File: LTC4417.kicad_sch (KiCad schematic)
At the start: 26 parts, among them Q4 IRF7324, Q5 IRF7324, Q6 IRF7324, Q7 IRF7324, U4 LTC4417CGN

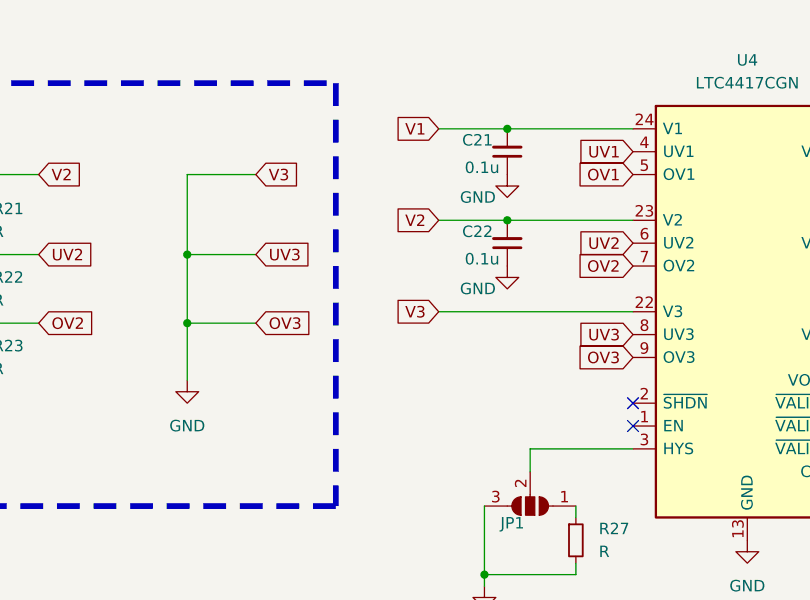
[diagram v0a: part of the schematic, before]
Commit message: LTC4088の修正必須
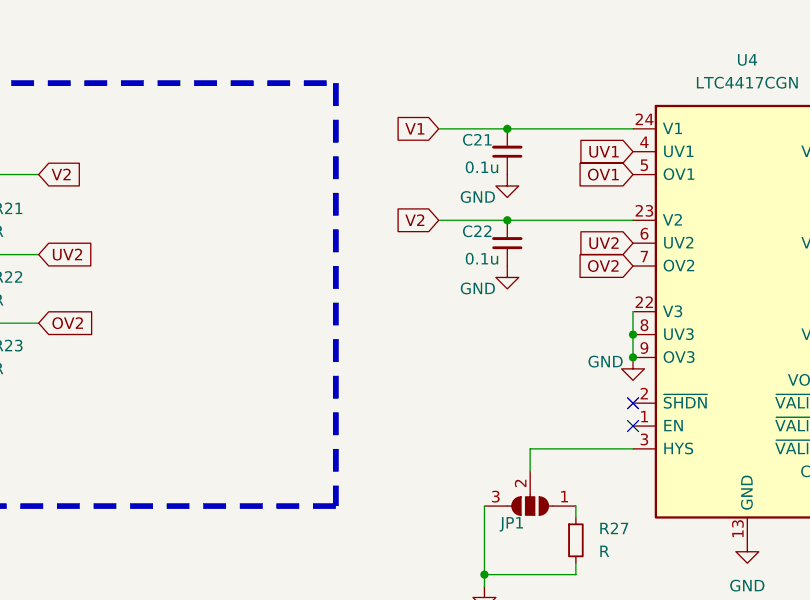
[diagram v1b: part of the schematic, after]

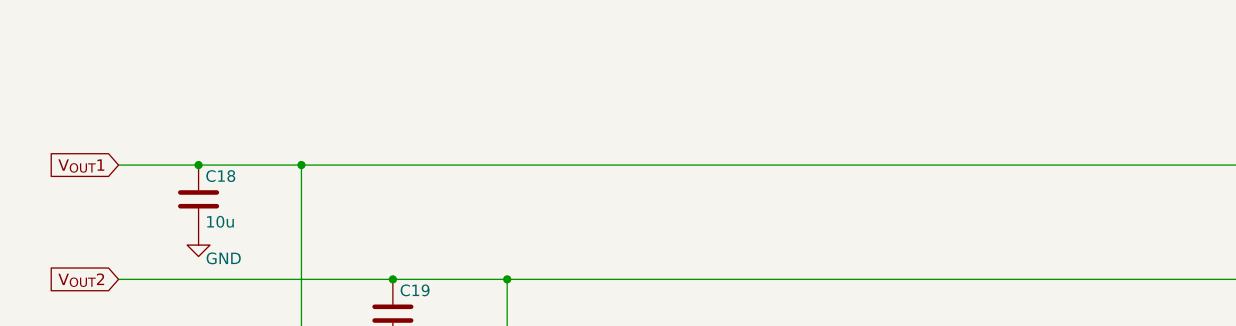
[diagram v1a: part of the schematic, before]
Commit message: add block image
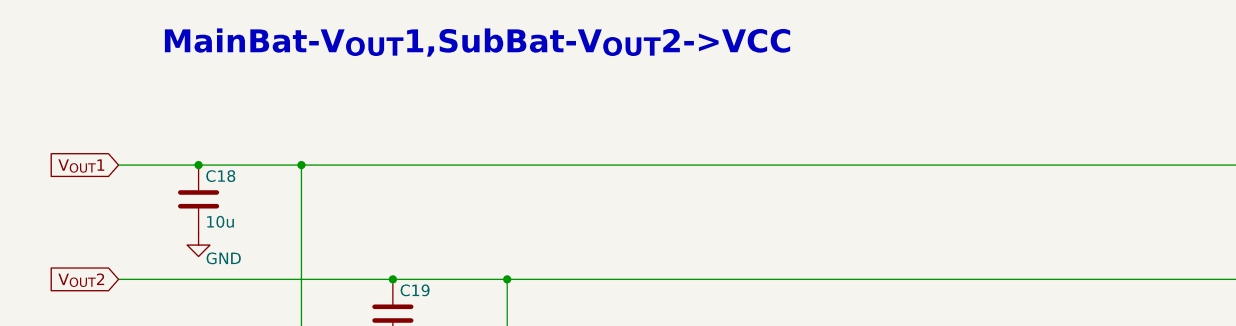
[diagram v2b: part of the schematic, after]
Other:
- note added: "MainBat-V_{OUT}1,SubBat-V_{OUT}2->VCC"
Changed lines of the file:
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@@
+		)
+	)
+	(text "MainBat-V_{OUT}1,SubBat-V_{OUT}2->VCC"
+		(exclude_from_sim no)
+		(at 32.766 25.908 0)
+		(effects
+			(font
+				(size 2.54 2.54)
+				(thickness 0.508)
+				(bold yes)
+			)
+			(justify left)
 		)
 	)

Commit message: update pcb
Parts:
- renumbered C18 to C1, C19 to C2, C21 to C3, C22 to C4, C24 to C5, C25 to C6, C27 to C7, C28 to C8, C29 to C9, D3 to D1, D4 to D2, Q4 to Q1, Q5 to Q2, Q6 to Q3, Q7 to Q4, R18 to R1, R19 to R2, R20 to R3, R21 to R4, R22 to R5, R23 to R6, R27 to R7, R28 to R8, R29 to R9, U4 to U1

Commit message: update pcb ltc4088kitsui
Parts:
- renumbered C1 to C11, C2 to C12, C3 to C13, C4 to C14, C5 to C15, C6 to C16, C7 to C17, C8 to C18, C9 to C19, D1 to D4, D2 to D5, Q1 to Q3, Q2 to Q4, Q3 to Q5, Q4 to Q6, R1 to R15, R2 to R16, R3 to R17, R4 to R18, R5 to R19, R6 to R20, R7 to R21, R8 to R22, R9 to R23, U1 to U2
